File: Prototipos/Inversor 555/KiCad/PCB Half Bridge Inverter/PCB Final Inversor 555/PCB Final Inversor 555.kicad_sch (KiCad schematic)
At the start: 18 parts, among them Q1 IRFZ44, Q2 IRFZ44, Q3 BC548, U1 TLC555xD, U2 LM7809_TO220

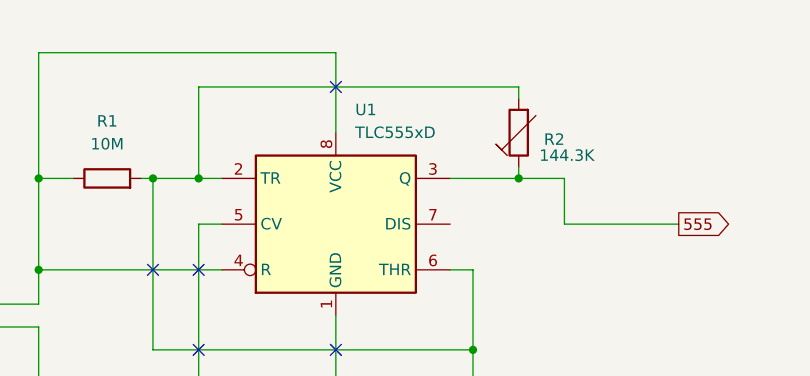
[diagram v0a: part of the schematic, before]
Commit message: Agregar resistencia en seria a potenciometro
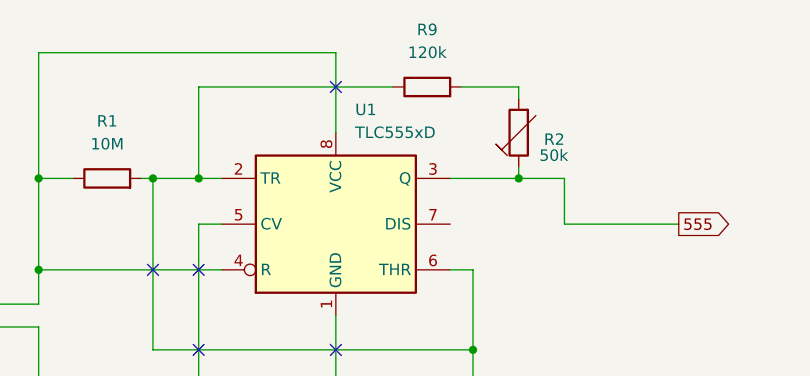
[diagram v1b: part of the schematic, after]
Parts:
- added R9: 120k, Resistor_THT:R_Axial_DIN0207_L6.3mm_D2.5mm_P7.62mm_Horizontal, symbol Device:R
- R2: value 144.3K -> 50k
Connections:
- net at C1.1, R1.2, U1.2 (TR)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: now also R9.1; no longer R2.2
- new net: R2.2, R9.2
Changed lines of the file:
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@@
+	(wire
+		(pts
+			(xy 71.12 52.07) (xy 92.71 52.07)
+		)
+		(stroke
+			(width 0)
+			(type default)
+		)
+	)
 	(wire
 		(pts
@@
 	(wire
 		(pts
-			(xy 106.68 52.07) (xy 71.12 52.07)
-		)
-		(stroke
-			(width 0)
-			(type default)
-		)
-	)
-	(wire
-		(pts
 			(xy 53.34 76.2) (xy 53.34 72.39)
 		)
@@
 		(pts
 			(xy 111.76 62.23) (xy 106.68 62.23)
+		)
+		(stroke
+			(width 0)
+			(type default)
+		)
+	)
+	(wire
+		(pts
+			(xy 100.33 52.07) (xy 106.68 52.07)
 		)
 		(stroke
@@
 			)
 		)
-		(property "Value" "144.3K"
+		(property "Value" "50k"
 			(at 108.966 59.69 0)
 			(effects
@@
 					(unit 1)
 				)
+			)
+		)
+	)
+	(symbol
+		(lib_id "Device:R")
+		(at 96.52 52.07 90)
+		(unit 1)
+		(exclude_from_sim no)
+		(in_bom yes)
+		(on_board yes)
+		(dnp no)
+		(fields_autoplaced yes)
+		(property "Reference" "R9"
+			(at 96.52 45.72 90)
+			(effects
+				(font
+					(size 1.27 1.27)
+				)
+			)
+		)
+		(property "Value" "120k"
+			(at 96.52 48.26 90)
+			(effects
+				(font
+					(size 1.27 1.27)
+				)
+			)
+		)
+		(property "Footprint" "Resistor_THT:R_Axial_DIN0207_L6.3mm_D2.5mm_P7.62mm_Horizontal"
+			(at 96.52 53.848 90)
+			(effects
+				(font
+					(size 1.27 1.27)
+				)
+				(hide yes)
+			)
+		)
+		(property "Datasheet" "~"
+			(at 96.52 52.07 0)
+			(effects
+				(font
+					(size 1.27 1.27)
+				)
+				(hide yes)
+			)
+		)
+		(property "Description" "Resistor"
+			(at 96.52 52.07 0)
+			(effects
+				(font
+					(size 1.27 1.27)
+				)
+				(hide yes)
+			)
+		)
+		(pin "2"
+		)
+		(pin "1"
+		)
+		(instances
+			(project "PCB Final Inversor 555"
+				(path "/9702be3b-5b84-4252-93e8-eb8d98955803"
+					(reference "R9")
+					(unit 1)
+				)

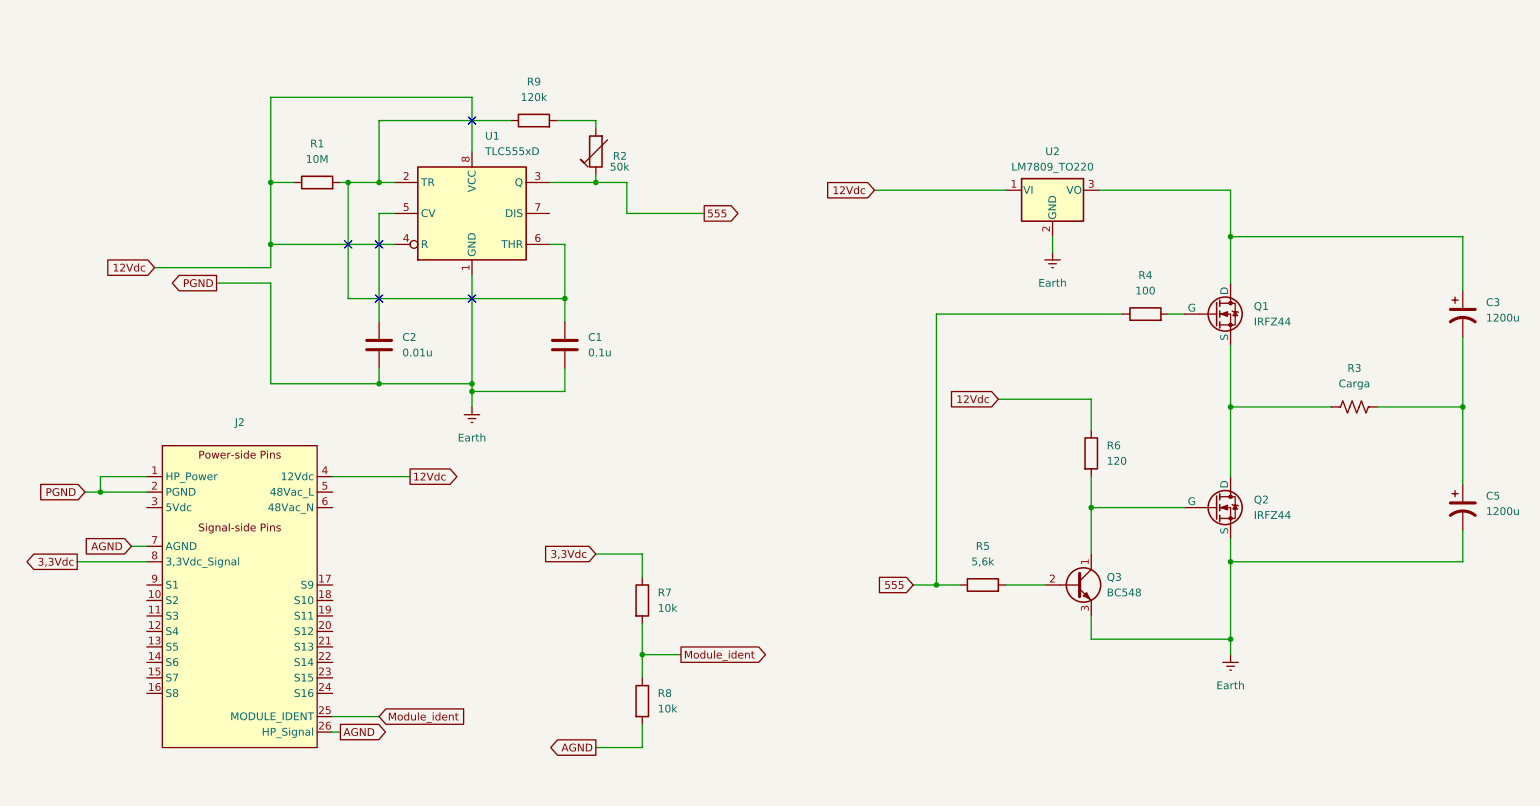
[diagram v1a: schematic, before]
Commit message: Agregar test point
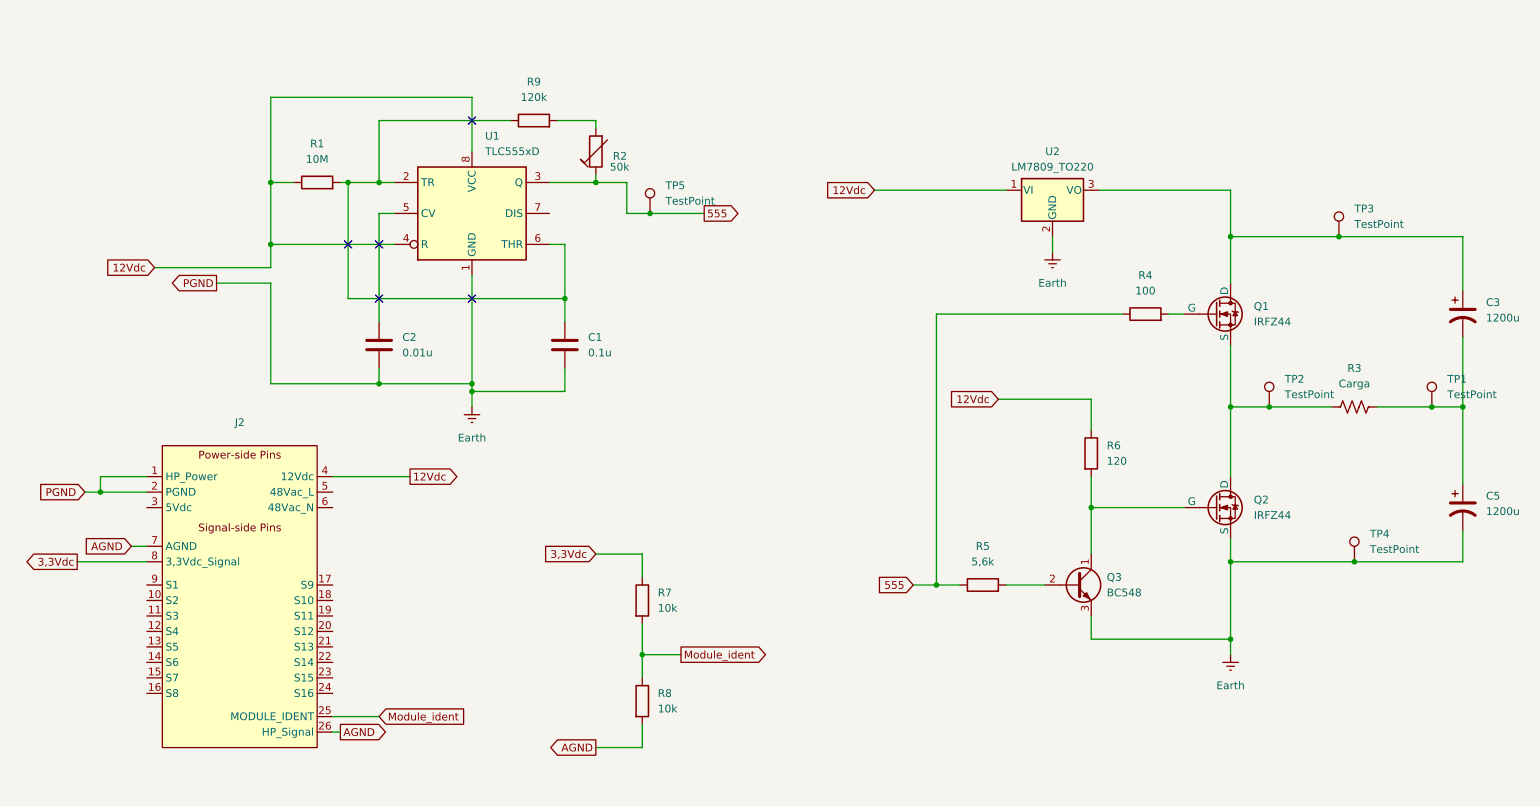
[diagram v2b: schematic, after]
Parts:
- added TP1, TP2, TP3, TP4, TP5: TestPoint, TestPoint:TestPoint_Loop_D1.80mm_Drill1.0mm_Beaded, symbol Connector:TestPoint
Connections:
- net 555: now also TP5.1
- net Earth: now also TP4.1
- net at C3.1, Q1.1 (D), U2.3 (VO): now also TP3.1
- net at Q1.3 (S), Q2.1 (D), R3.1: now also TP2.1
- net at C3.2, C5.1, R3.2: now also TP1.1

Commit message: Modificaciones en esquemático y PCB inversor medio puente.
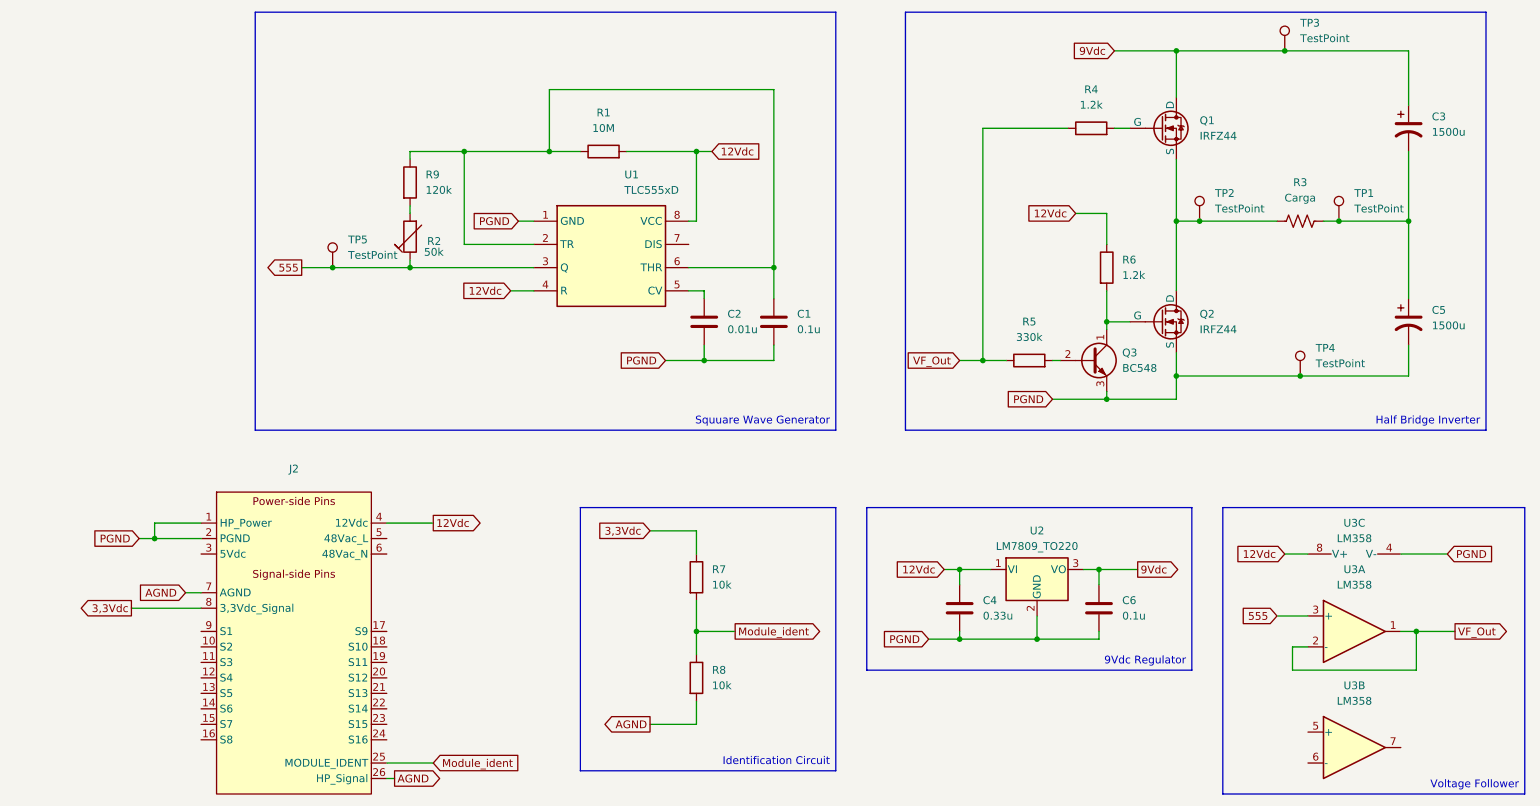
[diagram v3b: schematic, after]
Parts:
- added C4: 0.33u, Capacitor_THT:C_Disc_D3.8mm_W2.6mm_P2.50mm, symbol Device:C
- added C6: 0.1u, Capacitor_THT:C_Disc_D3.8mm_W2.6mm_P2.50mm, symbol Device:C
- added U3: LM358, Package_DIP:DIP-8_W7.62mm, symbol Amplifier_Operational:LM358
- C3, C5: value 1200u -> 1500u
- R4: value 100 -> 1.2k
- R5: value 5,6k -> 330k
- R6: value 120 -> 1.2k
- U1: footprint Package_DIP:DIP-8_W10.16mm -> Package_DIP:DIP-8_W7.62mm
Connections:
- net 12Vdc: now also R1.2, C4.1, U3.8 (V+); no longer R1.1
- net 555: now also U3.3 (+); no longer R4.1, R5.1
- net at C1.1, R9.1, U1.2 (TR)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: now also R1.1; no longer R1.2
- net 9Vdc: now reaches C3.1, Q1.1 (D), TP3.1, U2.3 (VO)
- net 9Vdc: now also C6.1
- net Earth renamed PGND
- net PGND: now also C4.2, C6.2, U3.4 (V-)
- new net VF_Out: R4.1, R5.1, U3.1, U3.2 (-)
- no-connect marks 5 -> 0
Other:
- company: (none) -> Alesandria - Cignetti - Galliano
- title: (none) -> PCB final Half Bridge Inverter
- moved on the sheet: C1, C2, C3, C5, J2, Q1, Q2, Q3, R1, R2, R3, R4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

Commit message: Corregir módulo inversor
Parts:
- R2: symbol Device:R_Trim -> Device:R_Variable
- R3: value Carga -> Load
- TP1: value TestPoint -> Load-
- TP2: value TestPoint -> Load+
- TP3: value TestPoint -> Regulator_output
- TP4: value TestPoint -> GND
- TP5: value TestPoint -> 555_OUT
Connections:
- net PGND is gone; now on net GND: C1.2, C2.2, C4.2, C5.2, C6.2, J2.1 (HP_Power), J2.2 (PGND), Q2.3 (S), Q3.3 (E), TP4.1, U1.1 (GND), U2.2 (GND), U3.4 (V-)
- net 555: now also R2.2; no longer R2.1
- net at R9.2: now also R2.1; no longer R2.2
- net AGND renamed GND
- no-connect marks 0 -> 3
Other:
- moved on the sheet: R2
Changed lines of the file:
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@@
 		)
 	)
-	(text_box "Squuare Wave Generator"
+	(text_box "Square Wave Generator"
 		(exclude_from_sim no)
 		(at 50.8 34.29 0)
@@
 		(color 0 0 0 0)
 	)
+	(no_connect
+		(at 223.52 157.48)
+	)
+	(no_connect
+		(at 223.52 152.4)
+	)
+	(no_connect
+		(at 238.76 154.94)
+	)
 	(wire
 		(pts
@@
 		)
 	)
-	(global_label "PGND"
+	(global_label "GND"
 		(shape input)
 		(at 118.11 91.44 180)
@@
 		)
 		(property "Intersheetrefs" "${INTERSHEET_REFS}"
-			(at 109.9843 91.44 0)
+			(at 111.2543 91.44 0)
 			(effects
 				(font
@@
 		)
 	)
-	(global_label "AGND"
+	(global_label "GND"
 		(shape output)
 		(at 115.57 151.13 180)
@@
 		)
 		(property "Intersheetrefs" "${INTERSHEET_REFS}"
-			(at 107.6257 151.13 0)
+			(at 108.7143 151.13 0)
 			(effects
 				(font
@@
 		)
 	)
-	(global_label "AGND"
+	(global_label "GND"
 		(shape output)
 		(at 73.66 160.02 0)
@@
 		)
 		(property "Intersheetrefs" "${INTERSHEET_REFS}"
-			(at 81.6043 160.02 0)
+			(at 80.5157 160.02 0)
 			(effects
 				(font
@@
 		)
 	)
-	(global_label "PGND"
+	(global_label "GND"
 		(shape input)
 		(at 31.75 120.65 180)
@@
 		)
 		(property "Intersheetrefs" "${INTERSHEET_REFS}"
-			(at 23.6243 120.65 0)
+			(at 24.8943 120.65 0)
 			(effects
 				(font
@@
 		)
 	)
-	(global_label "PGND"
+	(global_label "GND"
 		(shape input)
 		(at 246.38 123.19 0)
@@
 		)
 		(property "Intersheetrefs" "${INTERSHEET_REFS}"
-			(at 254.5057 123.19 0)
+			(at 253.2357 123.19 0)
 			(effects
 				(font
@@
 		)
 	)
-	(global_label "AGND"
+	(global_label "GND"
 		(shape input)
 		(at 39.37 129.54 180)
@@
 		)
 		(property "Intersheetrefs" "${INTERSHEET_REFS}"
-			(at 31.4257 129.54 0)
+			(at 32.5143 129.54 0)
 			(effects
 				(font
@@
 		)
 	)
-	(global_label "PGND"
+	(global_label "GND"
 		(shape input)
 		(at 93.98 68.58 180)
@@
 		)
 		(property "Intersheetrefs" "${INTERSHEET_REFS}"
-			(at 85.8543 68.58 0)
+			(at 87.1243 68.58 0)
 			(effects
 				(font
@@
 		)
 	)
-	(global_label "PGND"
+	(global_label "GND"
 		(shape input)
 		(at 161.29 137.16 180)
@@
 		)
 		(property "Intersheetrefs" "${INTERSHEET_REFS}"
-			(at 153.1643 137.16 0)
+			(at 154.4343 137.16 0)
 			(effects
 				(font
@@
 		)
 	)
-	(global_label "PGND"
+	(global_label "GND"
 		(shape input)
 		(at 181.61 97.79 180)
@@
 		)
 		(property "Intersheetrefs" "${INTERSHEET_REFS}"
-			(at 173.4843 97.79 0)
+			(at 174.7543 97.79 0)
 			(effects
 				(font
@@
 			)
 		)
-		(property "Value" "TestPoint"
+		(property "Value" "Load+"
 			(at 208.28 66.5479 0)
 			(effects
@@
 	)
 	(symbol
-		(lib_id "Device:R_Trim")
-		(at 76.2 71.12 180)
+		(lib_id "Device:R_Variable")
+		(at 76.2 71.12 0)
 		(unit 1)
 		(exclude_from_sim no)
@@
 		(dnp no)
 		(property "Reference" "R2"
-			(at 78.994 71.882 0)
+			(at 82.042 70.104 0)
 			(effects
 				(font
@@
 		)
 		(property "Value" "50k"
-			(at 78.486 73.66 0)
+			(at 83.058 72.136 0)
 			(effects
 				(font
@@
 		)
 		(property "Footprint" "Potentiometer_THT:Potentiometer_Alps_RK09K_Single_Vertical"
-			(at 77.978 71.12 90)
+			(at 74.422 71.12 90)
 			(effects
 				(font
@@
 			)
 		)
-		(property "Description" "Trimmable resistor (preset resistor)"
+		(property "Description" "Variable resistor"
 			(at 76.2 71.12 0)
 			(effects
@@
 			)
 		)
-		(property "Value" "Carga"
+		(property "Value" "Load"
 			(at 222.25 64.77 90)
 			(effects
@@
 			)
 		)
-		(property "Value" "TestPoint"
+		(property "Value" "Regulator_output"
 			(at 222.25 38.6079 0)
 			(effects
@@
 		(on_board yes)
 		(dnp no)
-		(fields_autoplaced yes)
 		(property "Reference" "TP5"
-			(at 66.04 71.6279 0)
+			(at 64.77 72.136 0)
 			(effects
 				(font
@@
 			)
 		)
-		(property "Value" "TestPoint"
-			(at 66.04 74.1679 0)
+		(property "Value" "555_OUT"
+			(at 64.77 74.422 0)
 			(effects
 				(font
@@
 			)
 		)
-		(property "Value" "TestPoint"
+		(property "Value" "Load-"
 			(at 231.14 66.5479 0)
 			(effects
@@
 			)
 		)
-		(property "Value" "TestPoint"
+		(property "Value" "GND"
 			(at 224.79 91.9479 0)
 			(effects
